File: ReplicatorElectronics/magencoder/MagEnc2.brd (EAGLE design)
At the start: 31.8 x 31.8 mm, 15 parts, among them IC2 AS5145

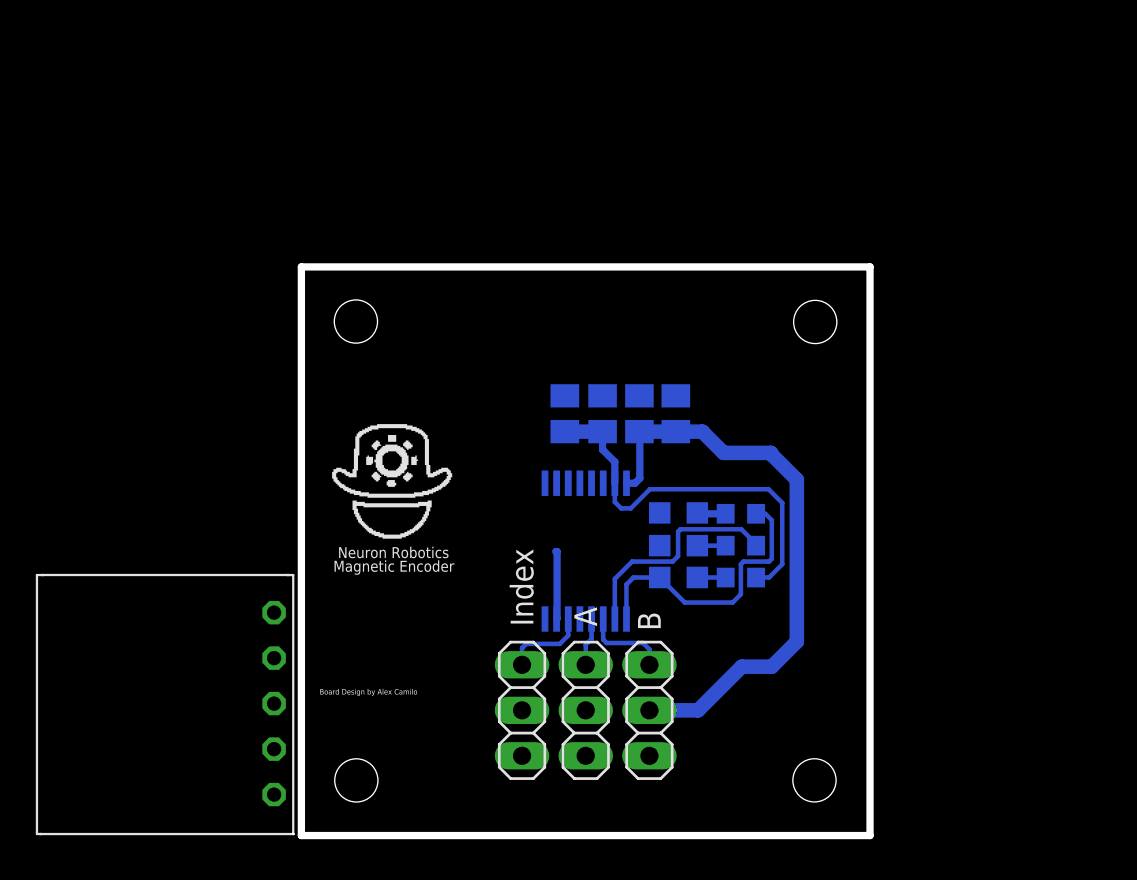
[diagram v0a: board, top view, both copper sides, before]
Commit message: 2/23/11: Added Rev. 3 of Encoder Board. This layout is complete, pending design changes which add pass-through servo control signals.
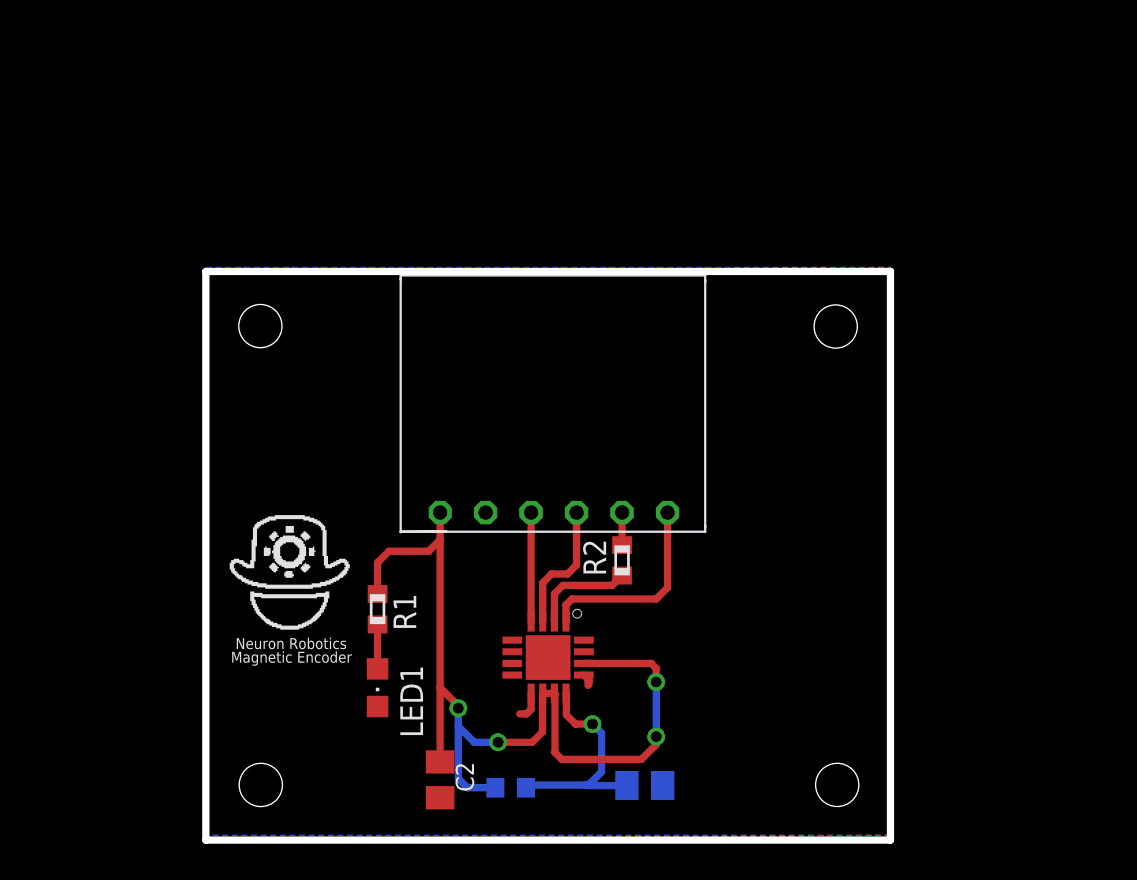
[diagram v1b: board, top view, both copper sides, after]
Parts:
- removed C3, C4: 10uf, rcl:C0805K
- removed IC2: AS5145, zo_TMS320DMC:SSOP16
- removed JP2, JP3, JP4: (no value), pinhead:1X03
- removed LED2: YELLOW, led:CHIPLED_0805
- removed LED3: RED, led:CHIPLED_0805
- added U$2: AS5055, AS5055:AS5055
- C1: value 10uf -> 4.7u
- C2: value 10uf -> 100n
- R2: value 680 -> 33
- R3: value 680 -> 15
- moved U$1 27.0 mm to (15.4, 23.1), turned to 270 degrees
- moved C2 21.6 mm to (7.75, 3.11), flipped to the top, turned to 270 degrees
- moved C1 20.9 mm to (19.2, 2.79), turned to 180 degrees
- moved R1 20.4 mm to (4.25, 12.6), flipped to the top, turned to 270 degrees
- moved R3 20.0 mm to (11.7, 2.67)
- moved LED1 17.9 mm to (4.25, 8.26), flipped to the top, turned to 180 degrees
- moved R2 6.68 mm to (17.9, 15.4), flipped to the top, turned to 90 degrees
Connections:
- removed net +3V3: C1.1, C2.1, IC2.15, R1.2
- removed net ENC_A: IC2.3, JP2.1
- removed net ENC_B: IC2.4, JP3.1
- removed net ENC_I: IC2.6, JP4.1
- removed net MAGDECN: IC2.2, R2.2
- removed net MAGINCN: IC2.1, LED1.C, R3.2
- removed net N$5: LED2.A, R3.1
- removed net SDO: IC2.9, U$1.P$5
- new net MISO: R2.2, U$1.P$5
- new net MOSI: U$1.P$6, U$2.1
- new net VDD: C1.1, R3.2, U$2.12
- net CSN: now also U$2.4; no longer IC2.11
- net GND: now also LED1.C, U$2.13, U$2.9; no longer C3.2, C4.2, IC2.7, IC2.8, JP2.3, JP3.3, JP4.3, LED2.C, LED3.C
- net N$1: now also R1.2; no longer R1.1
- net N$4: now also U$2.2; no longer LED3.A
- net SCLK: now also U$2.3; no longer IC2.10
- net VCC: now also C2.1, R1.1, R3.1, U$2.10, U$2.11, U$2.14; no longer C3.1, C4.1, IC2.16, JP2.2, JP3.2, JP4.2
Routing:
- net +3V3: track 21.8 -> 0.00 mm
- net VCC: track 32.3 -> 52.8 mm, vias 0 -> 4
- net MAGINCN: track 16.0 -> 0.00 mm
- net VDD: track 0.00 -> 12.7 mm, vias 0 -> 1
- net MAGDECN: track 12.5 -> 0.00 mm
- net MOSI: track 0.00 -> 11.2 mm
- net SCLK: track 0.00 -> 7.41 mm
- net CSN: track 0.00 -> 6.10 mm
- net ENC_A: track 4.82 -> 0.00 mm
- net ENC_I: track 4.73 -> 0.00 mm
- net N$4: track 1.58 -> 5.76 mm
- net ENC_B: track 2.69 -> 0.00 mm
- net MISO: track 0.00 -> 1.82 mm
- net N$5: track 1.63 -> 0.00 mm
- net GND: track 3.85 -> 2.62 mm
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- added copper zone on layer 1, net GND
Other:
- board size 31.8 x 31.8 mm -> 38.2 x 31.8 mm
- board text removed: "A"
- board text removed: "B"
- board text removed: "Board Design by Alex Camilo"
- board text removed: "Index"

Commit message: 3/7/12: Rev 4 of the Encoder Board. Added feed-through for servo, may yet need layout modifications to alter placement of encoder IC or size of mounting holes.
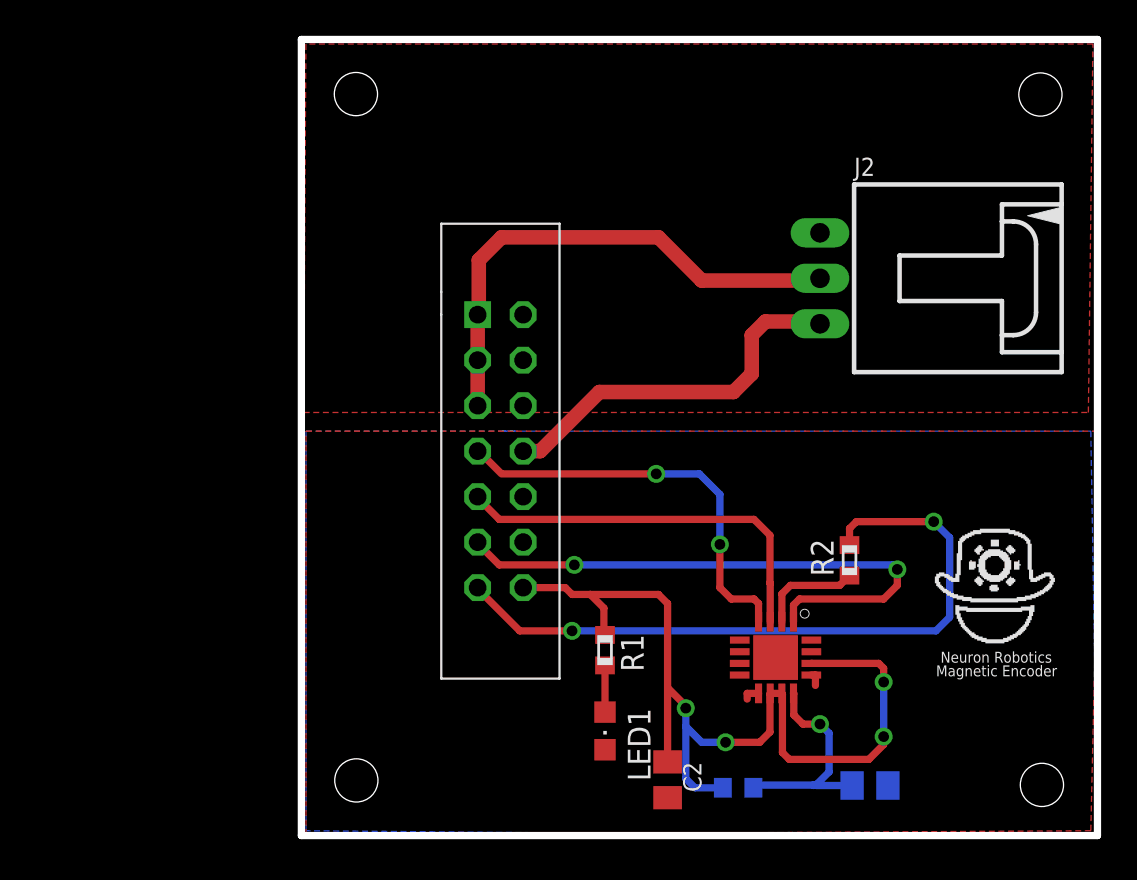
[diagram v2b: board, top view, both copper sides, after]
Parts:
- removed U$1: 70553-0106, 70553-0109:70553-0109
- added J1: SBH11-PBPC-D07-ST-BK, SBH11-PBPC-D07-ST-BK:SBH11-PBPC-D07-ST-BK
- added J2: 70553-0037, con-molex:70553-03
- moved LED1 12.9 mm to (17.0, 5.84)
- moved R1 12.9 mm to (17.0, 10.4)
- moved R3 12.7 mm to (24.4, 2.67)
- moved U$2 12.7 mm to (25.5, 11.9)
- moved C2 12.7 mm to (20.4, 3.11)
- moved R2 12.7 mm to (30.6, 15.4)
- moved C1 12.6 mm to (31.8, 2.79)
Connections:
- new net 5V_SERVO: J1.1, J1.3, J1.5, J2.2
- new net DGND: C1.2, C2.2, J1.10, J1.12, LED1.C, U$2.13, U$2.9
- new net SERVO_CTRL: J1.8, J2.3
- net CSN: now also J1.7; no longer U$1.P$3
- net GND: now also J1.2, J1.4, J1.6, J2.1; no longer C1.2, C2.2, LED1.C, U$1.P$2, U$2.13, U$2.9
- net MISO: now also J1.13; no longer U$1.P$5
- net MOSI: now also J1.11; no longer U$1.P$6
- net SCLK: now also J1.9; no longer U$1.P$4
- net VCC: now also J1.14; no longer U$1.P$1
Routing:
- net MISO: track 1.82 -> 39.3 mm, vias 0 -> 2
- net 5V_SERVO: track 0.00 -> 28.8 mm
- net MOSI: track 11.2 -> 32.2 mm, vias 0 -> 2
- net SERVO_CTRL: track 0.00 -> 20.9 mm
- net CSN: track 6.10 -> 23.3 mm, vias 0 -> 2
- net SCLK: track 7.41 -> 22.1 mm
- net GND: track 2.62 -> 0.00 mm
- net DGND: track 0.00 -> 1.76 mm
- net VCC: track 52.8 -> 53.7 mm
- added copper zone on layer 1, net DGND
- added copper zone on layer 16, net DGND
- removed copper zone on layer 16, net GND
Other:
- board size 38.2 x 31.8 mm -> 44.5 x 44.5 mm

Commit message: 3/17/12: Rev. 5 of the Encoder Board. Moved connectors to back side of board, centered encoder on board, changed clearance hole size to fit 8-32 screws.
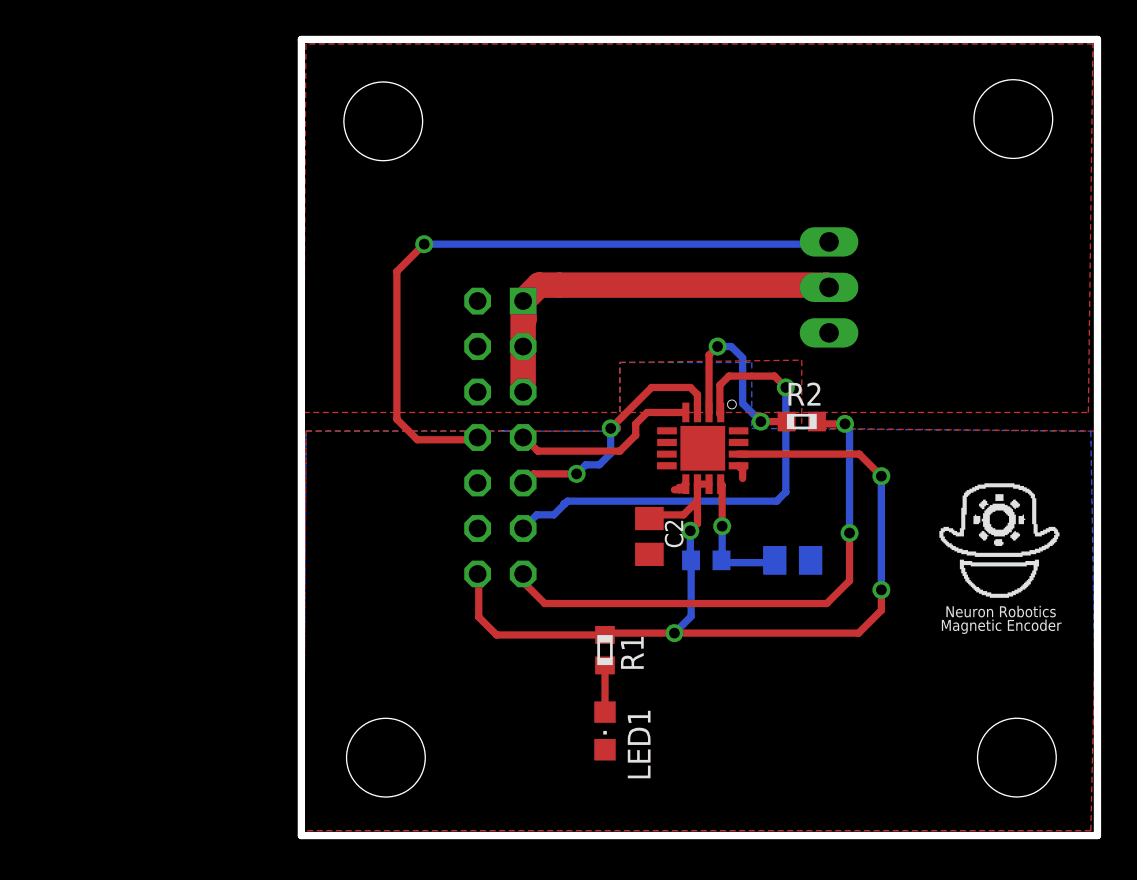
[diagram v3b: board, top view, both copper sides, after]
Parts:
- moved C2 13.6 mm to (19.4, 16.7)
- moved C1 13.3 mm to (27.4, 15.4)
- moved R3 12.8 mm to (22.6, 15.4)
- moved U$2 12.4 mm to (21.5, 23.6)
- moved R2 8.19 mm to (27.9, 23.1), turned to 0 degrees
- moved J1 2.65 mm to (12.4, 29.8), flipped to the bottom
- moved J2 0.72 mm to (37.1, 30.6), flipped to the bottom, turned to 90 degrees
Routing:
- net SERVO_CTRL: track 20.9 -> 38.3 mm, vias 0 -> 1
- net CSN: track 23.3 -> 10.7 mm, vias 2 -> 0
- net MISO: track 39.3 -> 30.2 mm
- net SCLK: track 22.1 -> 13.9 mm, vias 0 -> 2
- net N$4: track 5.76 -> 11.4 mm, vias 0 -> 2
- net 5V_SERVO: track 28.8 -> 23.5 mm
- net MOSI: track 32.2 -> 27.3 mm, vias 2 -> 1
- net VDD: track 12.4 -> 7.56 mm
- net DGND: track 1.76 -> 2.96 mm
- net VCC: track 53.7 -> 54.6 mm

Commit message: 3/31/12: Rev. 6 of the Encoder board. Modified 2x7 pin header decal, moved location of 1x3 pin header, generated DXF files (one with just mounting holes, another with holes and high-profile components).
~ 0.5 hrs invested.
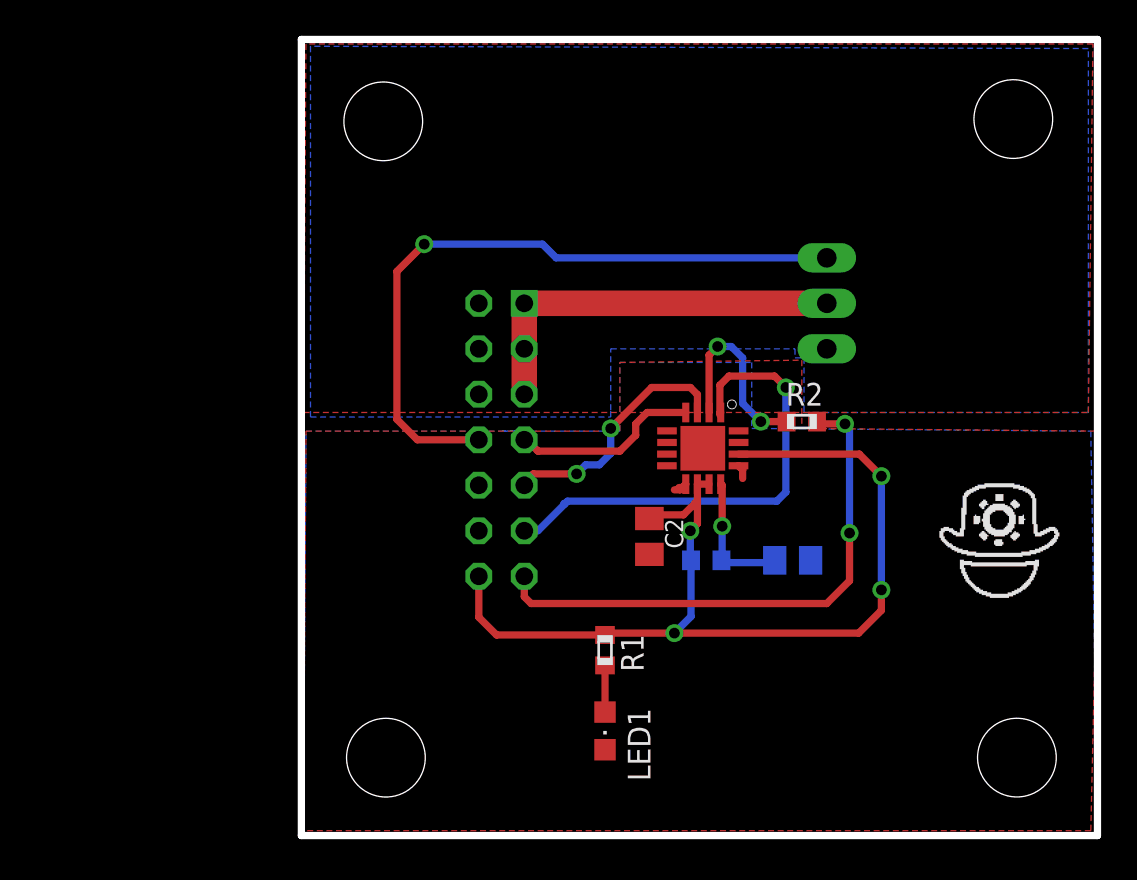
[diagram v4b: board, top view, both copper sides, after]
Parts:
- moved J2 0.90 mm to (37.0, 29.7)
- moved J1 0.14 mm to (12.4, 29.7)
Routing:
- net 5V_SERVO: track 23.5 -> 22.0 mm
- added copper zone on layer 16, net GND
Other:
- board text added: "Francesco Bivona"
- board text added: "Mounting holes are 8-32 (0.173")"
- board text added: "Rev. 5"
